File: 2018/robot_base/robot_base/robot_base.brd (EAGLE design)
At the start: 94.2 x 74.4 mm, 41 parts

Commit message: Finished wiring using top layer jumpers
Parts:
- moved R5 12.2 mm to (88.9, 21.3)
- moved R4 10.8 mm to (91.7, 21.6)
- moved JP_UART4 1.78 mm to (83.8, 15.2)
- moved JP11 1.76 mm to (81.8, 66.2), turned to 180 degrees
- moved JP_5V 1.27 mm to (88.9, 59.7)
- turned R1 to 270 degrees
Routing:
- net I2C0_VCC: track 16.6 -> 159.7 mm, vias 0 -> 6
- net 3V3: track 79.5 -> 175.6 mm, vias 0 -> 10
- net SCL0: track 8.72 -> 70.0 mm, vias 0 -> 6
- net SDA0: track 4.47 -> 55.0 mm, vias 0 -> 4
- net SDA1: track 11.6 -> 47.8 mm, vias 0 -> 2
- net SCL1: track 14.9 -> 50.8 mm, vias 0 -> 2
- net GND: track 95.5 -> 121.5 mm, vias 0 -> 14
- net I2C1_VCC: track 14.6 -> 37.8 mm, vias 0 -> 2
- net CUR3_SE: track 0.00 -> 20.1 mm, vias 0 -> 2
- net RX4: track 3.20 -> 14.9 mm
- net 5V: track 313.4 -> 321.0 mm
- net CUR1_SE: track 38.4 -> 44.1 mm
- net N$52: track 50.6 -> 44.9 mm
- net N$58: track 23.8 -> 28.4 mm
- net N$5: track 69.2 -> 72.4 mm
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
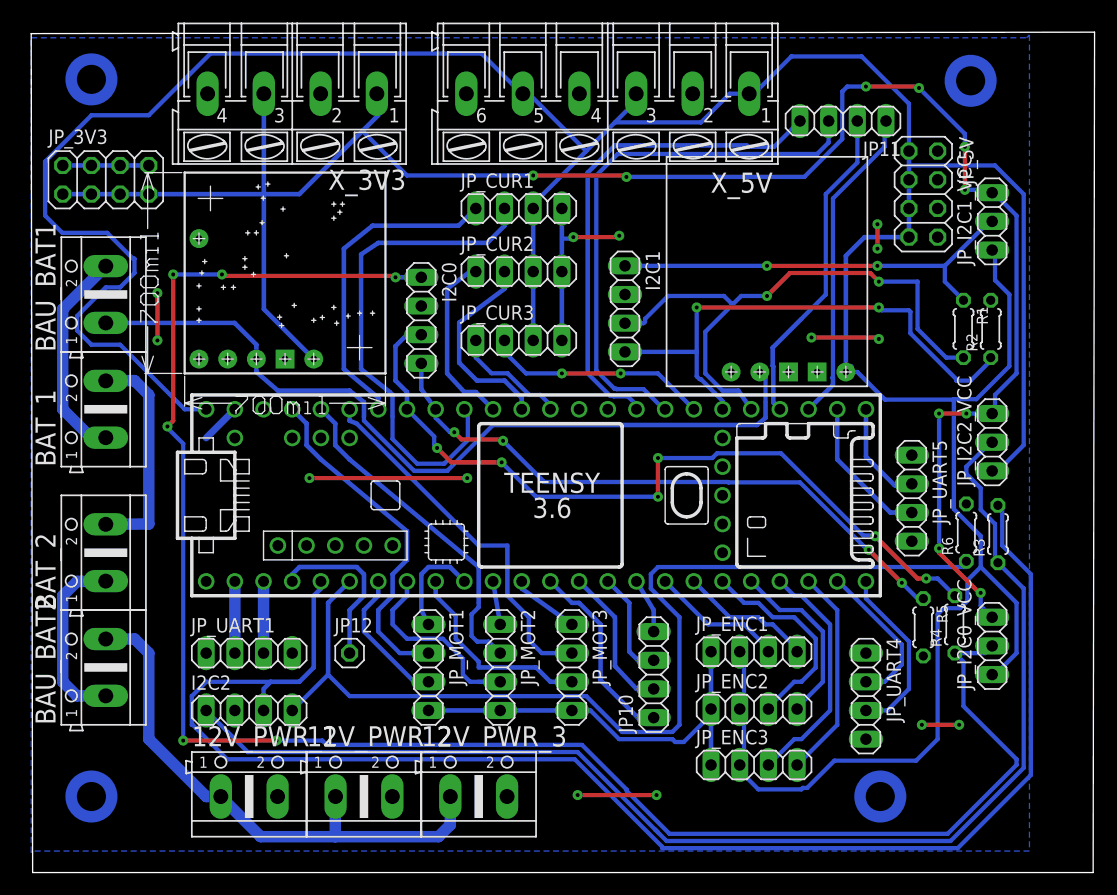
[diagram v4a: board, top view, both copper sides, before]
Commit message: robot_base.sch/brd: routing complete, clearance increased and checked. Add teensy package with bigger pads.
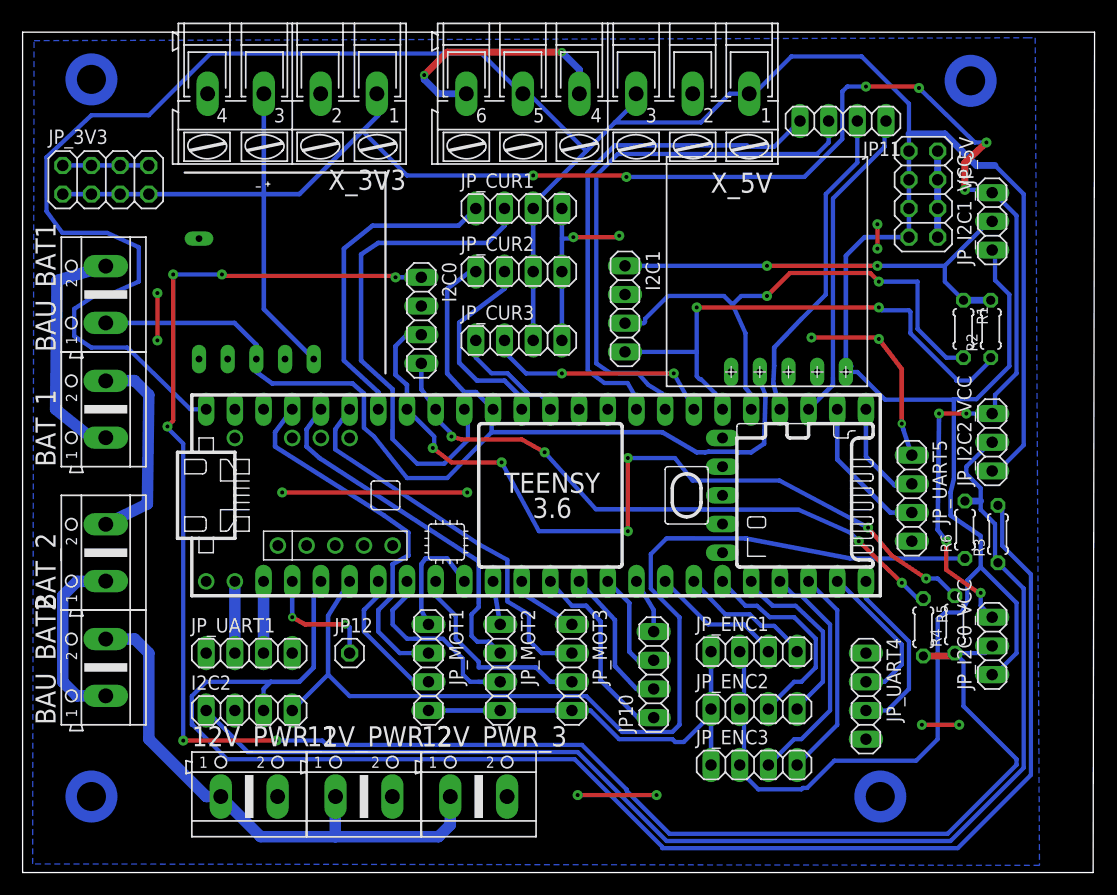
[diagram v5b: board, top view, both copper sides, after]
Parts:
- U$1: value TEENSY_3.5/3.6 -> TEENSY_3.5/3.6TEENSY_3.5/3.6_LONG_PADS
- moved R6 0.28 mm to (92.6, 30.0)
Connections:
- removed net 3V3_TEESNY_1: U$1.3V3_LO
- removed net N$28: U$1.U5V
- removed net N$29: U$1.UD-
- removed net N$30: U$1.UD+
- removed net N$31: U$1.UGND1
- removed net N$32: U$1.UGND2
- removed net N$33: U$1.A11
- removed net N$34: U$1.A10
- removed net N$35: U$1.AREF
- removed net N$36: U$1.VUSB
- removed net N$61: U$1.RESET
- removed net N$62: U$1.PROG
- removed net N$63: U$1.GND3
- removed net N$64: U$1.3V3_2
- removed net N$65: U$1.VBAT
- net I2C0_VCC: now also R5.2
- net I2C1_VCC: now also R2.2
- net I2C2_VCC: now also R6.2
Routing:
- net GND: track 121.5 -> 159.6 mm, vias 14 -> 17
- net CUR3_SE: track 20.1 -> 25.3 mm
- net SCL0: track 70.0 -> 74.6 mm
- net N$5: track 72.4 -> 76.8 mm
- net N$7: track 15.0 -> 10.8 mm, vias 0 -> 2
- net 5V: track 321.0 -> 324.7 mm
- net SCL1: track 50.8 -> 47.8 mm
- net I2C0_VCC: track 159.7 -> 162.6 mm
- net MOT1_IN_B: track 31.2 -> 33.9 mm
- net I2C1_VCC: track 37.8 -> 40.3 mm
- net MOT2_IN_B: track 29.9 -> 32.1 mm
- net N$8: track 19.1 -> 21.2 mm
- net 3V3: track 175.6 -> 177.6 mm
- net MOT3_IN_B: track 33.0 -> 34.6 mm
- net SDA2: track 90.1 -> 91.5 mm
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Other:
- board size 94.2 x 74.4 mm -> 94.9 x 74.4 mm

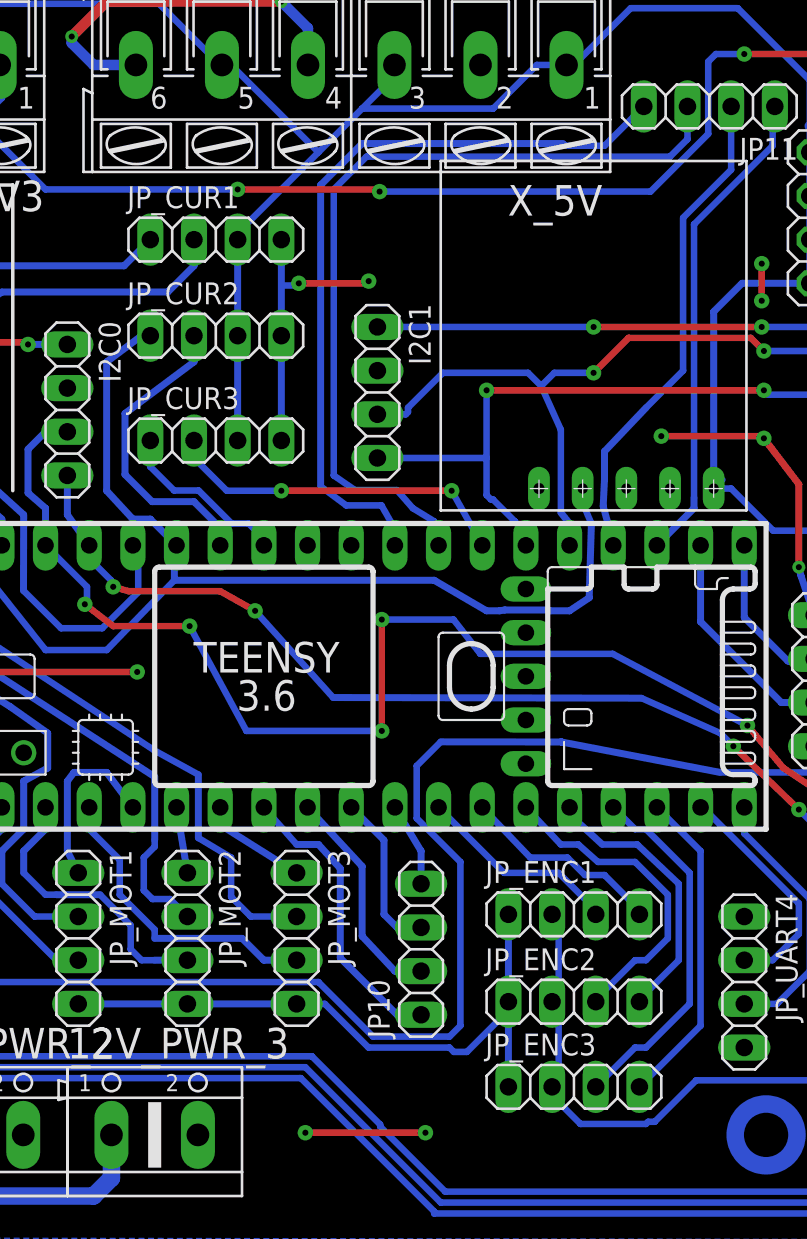
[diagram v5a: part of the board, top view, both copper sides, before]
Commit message: Correction of traces Overlap issues
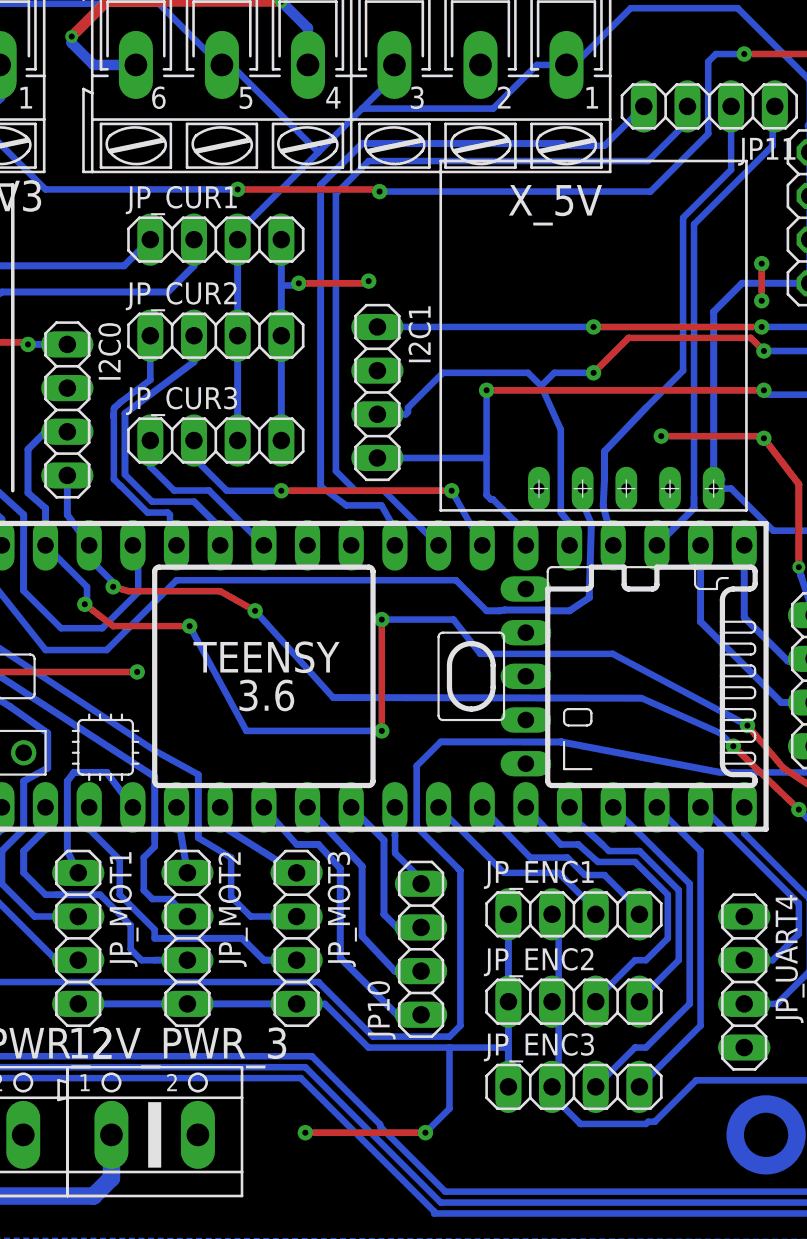
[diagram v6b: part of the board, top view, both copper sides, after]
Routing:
- net CUR3_SE: track 25.3 -> 20.4 mm
- net GND: track 159.6 -> 164.0 mm
- net N$53: track 48.7 -> 47.0 mm

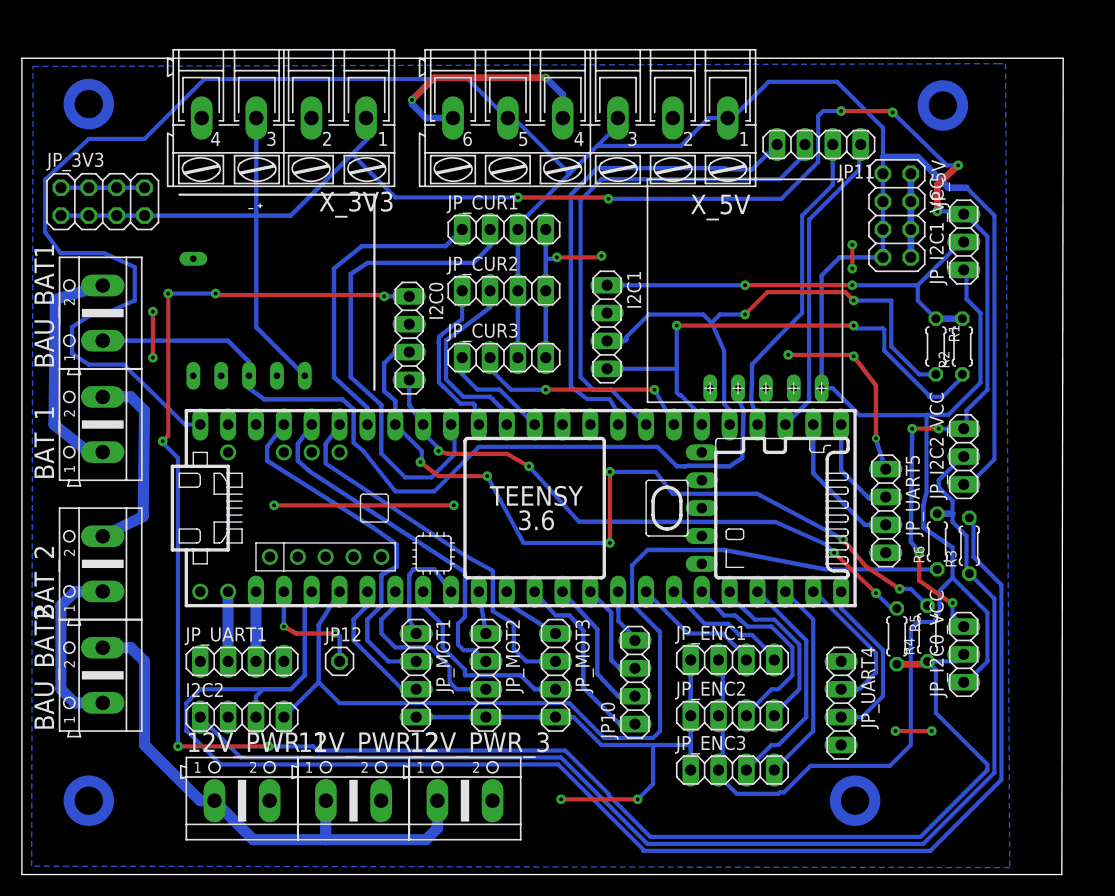
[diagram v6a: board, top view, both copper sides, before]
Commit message: [robot_base] Update robot_base and robot_systems boards.
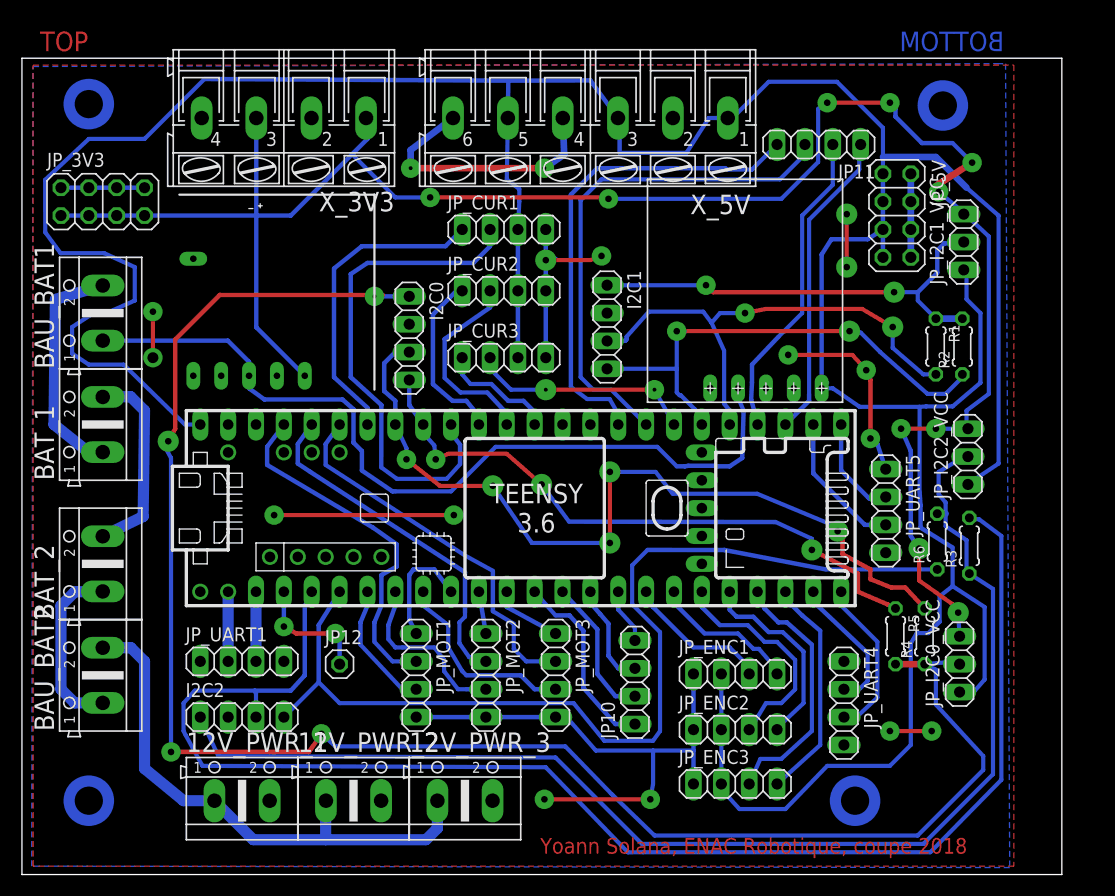
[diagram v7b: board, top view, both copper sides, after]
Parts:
- moved JP_ENC3 1.30 mm to (74.2, 7.87)
- moved JP_ENC1 1.30 mm to (74.2, 17.9)
- moved JP_ENC2 1.30 mm to (74.2, 12.8)
- moved JP_I2C0_VCC 0.97 mm to (94.6, 18.8)
- moved JP_I2C2_VCC 0.38 mm to (95.4, 37.7)
- moved R4 0.36 mm to (91.4, 21.3)
- moved JP_UART4 0.25 mm to (84.1, 15.2)
- moved JP12 0.25 mm to (38.1, 18.8)
- moved R5 0.13 mm to (88.8, 21.3)
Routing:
- net GND: track 164.0 -> 173.4 mm
- net 5V: track 324.7 -> 331.8 mm
- net 3V3: track 177.6 -> 182.0 mm
- net SCL1: track 47.8 -> 45.2 mm
- net ENC3_A: track 20.7 -> 23.3 mm
- net SDA1: track 47.8 -> 45.4 mm
- net ENC3_B: track 18.8 -> 21.2 mm
- net ENC2_B: track 15.9 -> 18.0 mm
- net SDA0: track 54.6 -> 56.7 mm, vias 4 -> 3
- net CUR1_SE: track 44.1 -> 46.0 mm
- net ENC2_A: track 18.7 -> 20.6 mm
- net SCL0: track 74.6 -> 76.3 mm, vias 6 -> 5
- net ENC1_B: track 11.9 -> 13.4 mm
- net SCL2: track 131.7 -> 133.2 mm
- net ENC1_A: track 11.8 -> 13.2 mm
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- added copper zone on layer 1, net GND
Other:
- board size 94.9 x 74.4 mm -> 94.8 x 74.4 mm
- board text added: "BOTTOM"
- board text added: "TOP"
- board text added: "Yoann Solana, ENAC Robotique, coupe 2018"

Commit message: [robot_base] Update dimensions of robot_base board
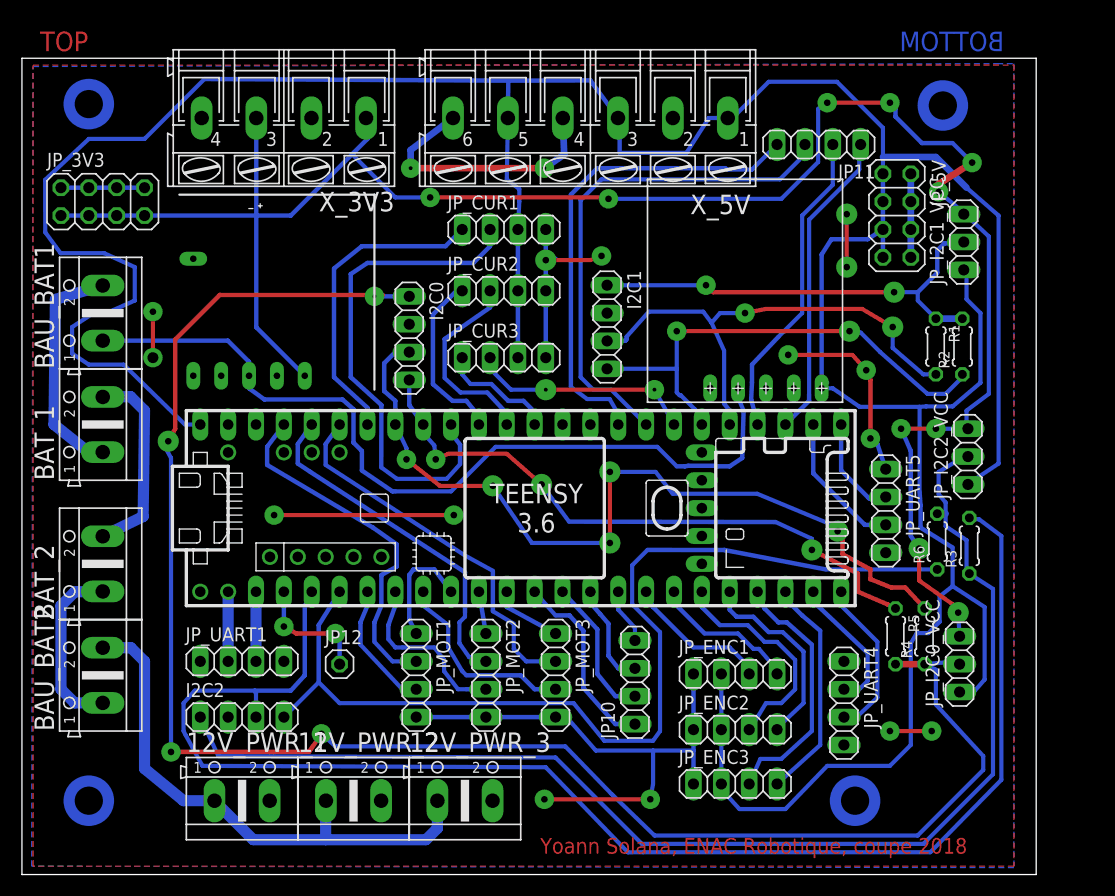
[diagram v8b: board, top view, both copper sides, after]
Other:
- board size 94.8 x 74.4 mm -> 92.5 x 74.4 mm
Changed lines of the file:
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@@
 <board>
 <plain>
-<wire x1="9.144" y1="-0.381" x2="103.937" y2="-0.381" width="0" layer="20"/>
-<wire x1="103.937" y1="-0.381" x2="103.937" y2="74.031" width="0" layer="20"/>
-<wire x1="103.937" y1="74.031" x2="9.144" y2="74.031" width="0" layer="20"/>
+<wire x1="9.144" y1="-0.381" x2="101.6" y2="-0.381" width="0" layer="20"/>
+<wire x1="101.6" y1="-0.381" x2="101.6" y2="74.031" width="0" layer="20"/>
+<wire x1="101.6" y1="74.031" x2="9.144" y2="74.031" width="0" layer="20"/>
 <wire x1="9.144" y1="74.031" x2="9.144" y2="-0.381" width="0" layer="20"/>
 <circle x="15.24" y="69.85" radius="1.79605" width="1.016" layer="16"/>
@@
 <vertex x="10.16" y="73.279"/>
 <vertex x="98.044" y="73.533"/>
-<vertex x="98.806" y="73.533"/>
-<vertex x="99.187" y="0.254"/>
+<vertex x="99.568" y="73.533"/>
+<vertex x="99.568" y="0.254"/>
 </polygon>
 <via x="32.131" y="32.385" extent="1-16" drill="0.6" diameter="1.778"/>
@@
 </signal>
 </signals>
-<errors>
-</errors>
 </board>
 </drawing>
